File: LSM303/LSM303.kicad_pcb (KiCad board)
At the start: 2 copper layers, 25.4 x 17.8 mm, 26 parts, among them J1 Conn_01x06, J2 Conn_01x04, J3 Conn_01x06, J4 Conn_01x04, Q2 BSS138DW, U1 AP2127K-3.3, U2 LSM303AGR

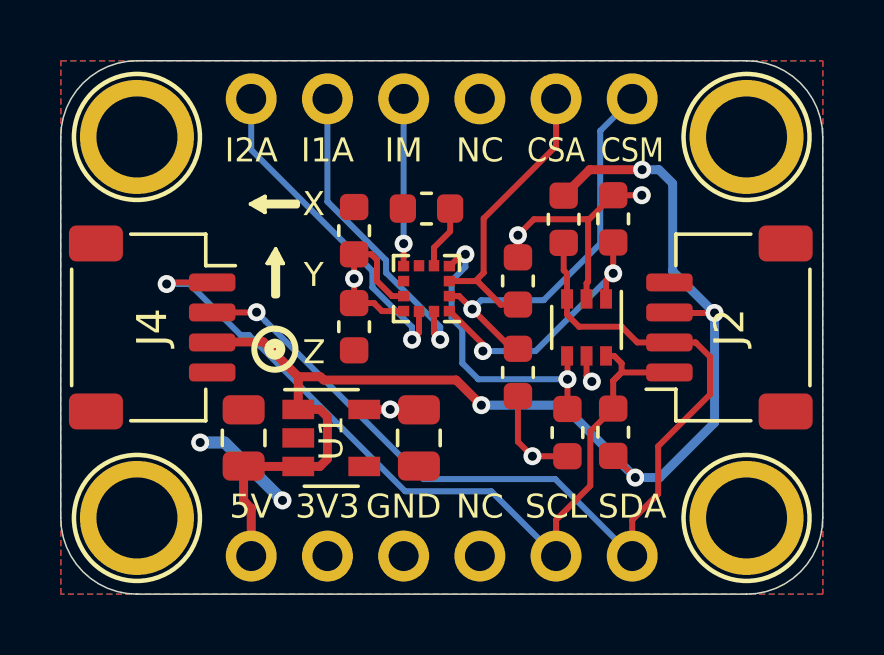
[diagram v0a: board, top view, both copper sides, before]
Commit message: Copper Pour Edits
Copper pour reduced to have 0.2mm edge clearance
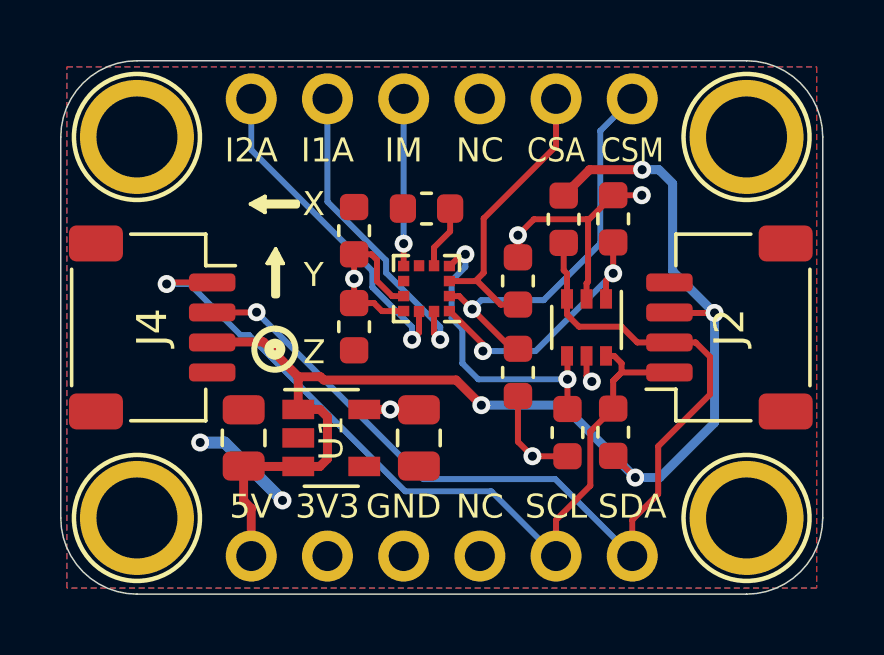
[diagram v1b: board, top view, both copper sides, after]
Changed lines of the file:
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@@
   )
   (setup
-    (last_trace_width 0.4)
+    (last_trace_width 0.127)
     (user_trace_width 0.2)
     (user_trace_width 0.25)
@@
     (polygon
       (pts
-        (xy 52.578 27.0764) (xy 77.978 27.0764) (xy 77.978 44.8564) (xy 52.578 44.8564)
+        (xy 52.7812 27.2796) (xy 77.7748 27.2796) (xy 77.7748 44.6532) (xy 52.7812 44.6532)
       )
     )
@@
     (polygon
       (pts
-        (xy 52.578 27.0764) (xy 77.978 27.0764) (xy 77.978 44.8564) (xy 52.578 44.8564)
+        (xy 52.7812 27.2796) (xy 77.7748 27.2796) (xy 77.7748 44.6532) (xy 52.7812 44.6532)
       )
     )

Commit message: Soldermask width adjusted
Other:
- rule solder_mask_min_width: 0.1 -> 0.05
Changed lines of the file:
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@@
     (pad_drill 1)
     (pad_to_mask_clearance 0)
-    (solder_mask_min_width 0.1)
+    (solder_mask_min_width 0.05)
     (aux_axis_origin 0 0)
     (visible_elements 7FFFFFFF)
